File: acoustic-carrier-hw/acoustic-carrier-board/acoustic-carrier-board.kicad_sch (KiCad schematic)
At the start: 0 parts

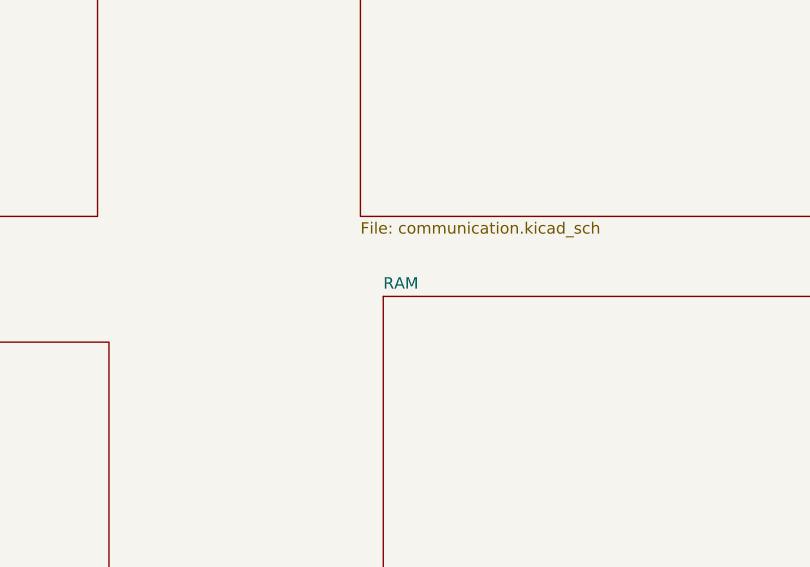
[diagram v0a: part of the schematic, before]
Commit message: [carrier] Finished ethernet
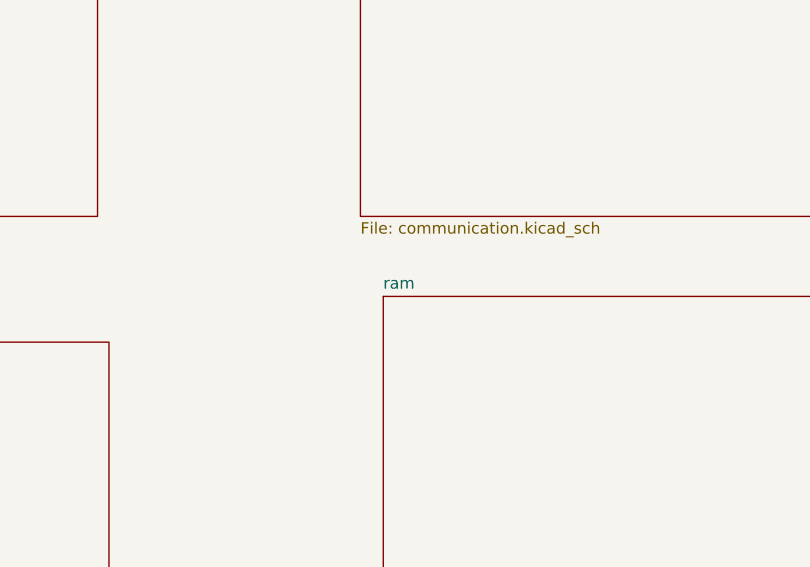
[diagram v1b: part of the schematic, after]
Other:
- sheet RAM renamed ram
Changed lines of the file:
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@@
 			(color 0 0 0 0.0000)
 		)
-		(property "Sheetname" "RAM"
+		(property "Sheetname" "ram"
 			(at 177.8 122.4784 0)
 			(effects

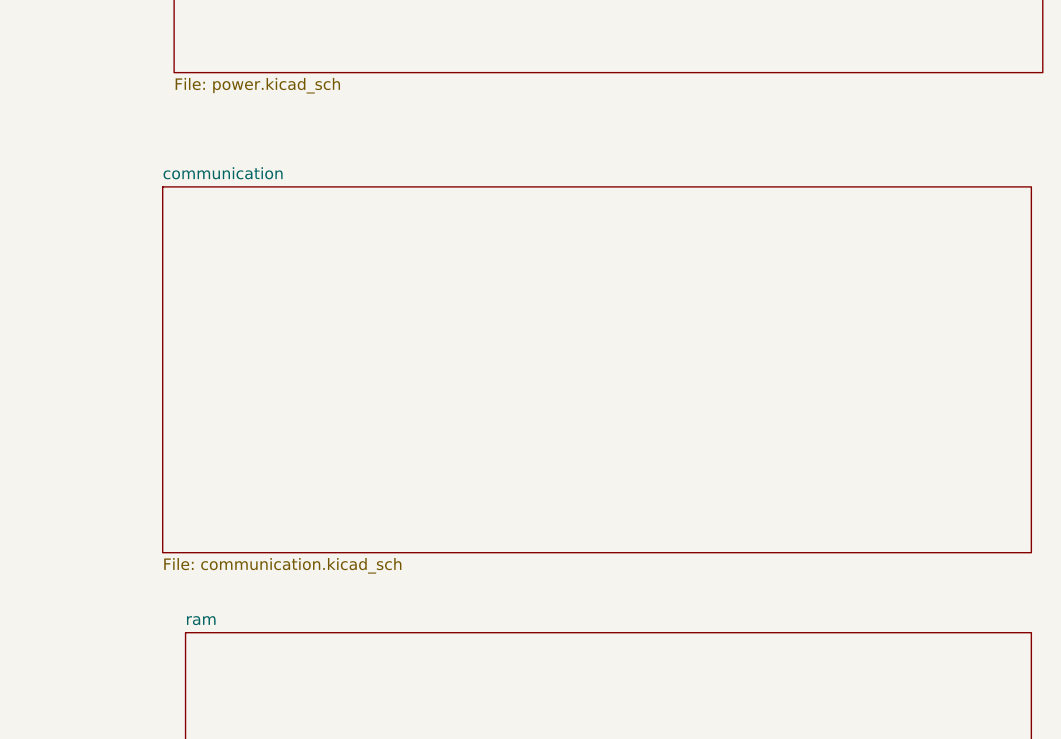
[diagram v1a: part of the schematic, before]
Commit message: [carrier] Fixed most of the carrier board ERC issues (next) fix BGA ERC issue
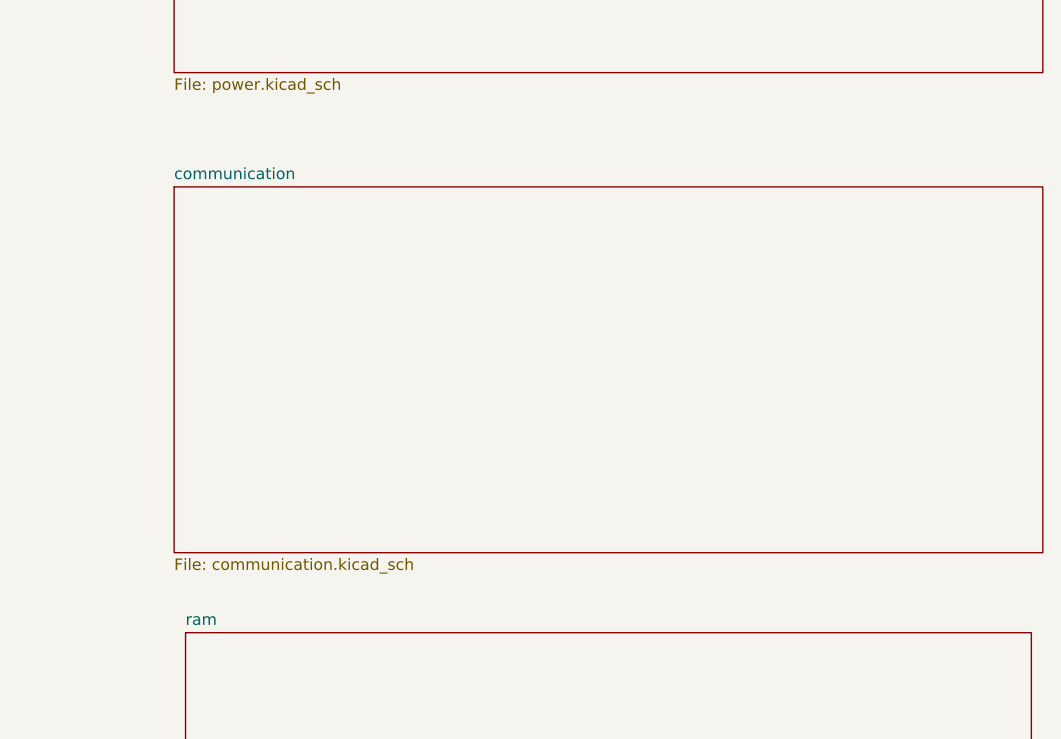
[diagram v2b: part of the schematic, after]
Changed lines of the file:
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@@
 	)
 	(sheet
-		(at 175.26 73.66)
+		(at 176.53 73.66)
 		(size 96.52 40.64)
 		(exclude_from_sim no)
@@
 		)
 		(property "Sheetname" "communication"
-			(at 175.26 72.9484 0)
+			(at 176.53 72.9484 0)
 			(effects
 				(font
@@
 		)
 		(property "Sheetfile" "communication.kicad_sch"
-			(at 175.26 114.8846 0)
+			(at 176.53 114.8846 0)
 			(effects
 				(font
@@
 		)
 		(property "Field2" ""
-			(at 175.26 73.66 0)
+			(at 176.53 73.66 0)
 			(effects
 				(font

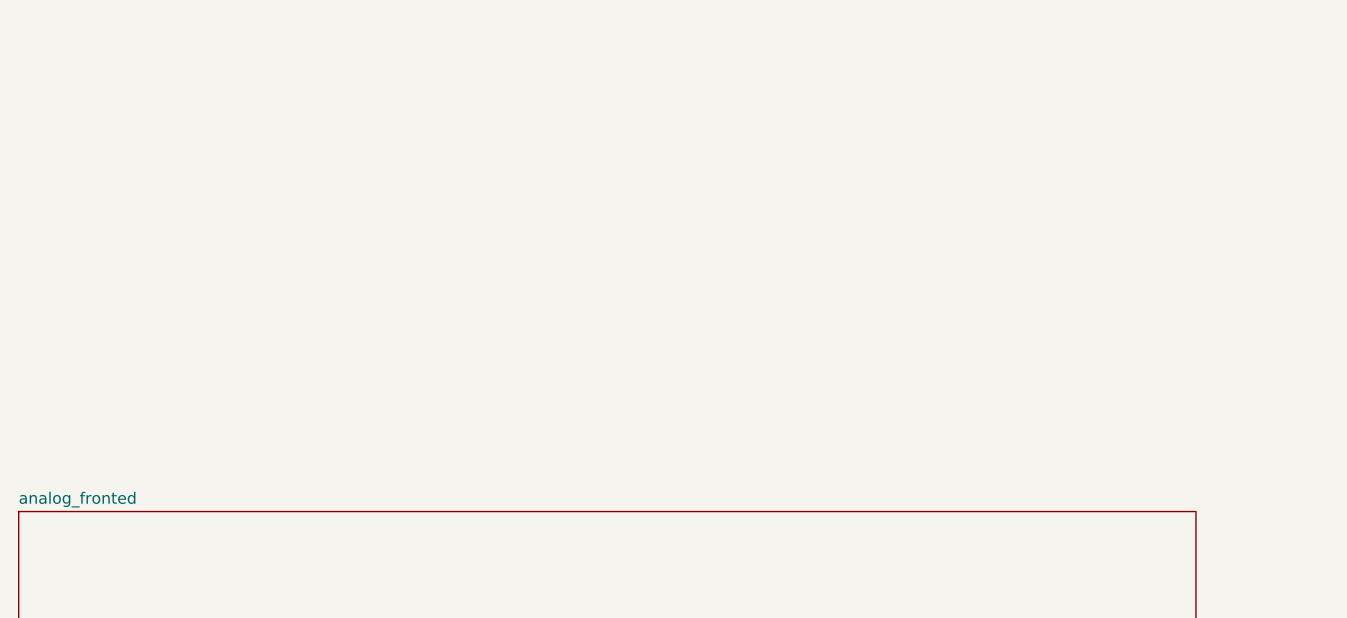
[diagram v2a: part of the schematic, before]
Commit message: [carrier] Fixed ERC errors and fpga-footprints (next) ) add extra pin functionality to 2 remaining banks, perform schematic checks
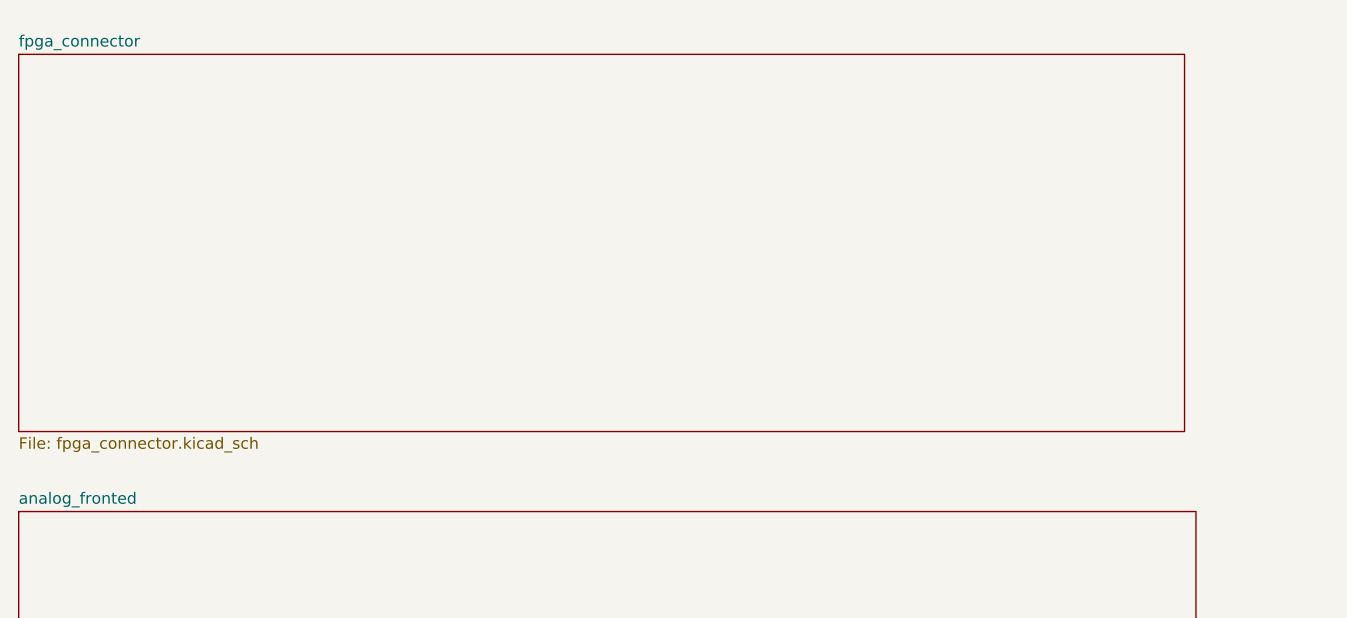
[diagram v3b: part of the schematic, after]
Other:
- added sheet fpga_connector (fpga_connector.kicad_sch)
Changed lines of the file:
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@@
+	)
+	(sheet
+		(at 15.24 24.13)
+		(size 129.54 41.91)
+		(exclude_from_sim no)
+		(in_bom yes)
+		(on_board yes)
+		(dnp no)
+		(fields_autoplaced yes)
+		(stroke
+			(width 0.1524)
+			(type solid)
+		)
+		(fill
+			(color 0 0 0 0.0000)
+		)
+		(property "Sheetname" "fpga_connector"
+			(at 15.24 23.4184 0)
+			(effects
+				(font
+					(size 1.27 1.27)
+				)
+				(justify left bottom)
+			)
+		)
+		(property "Sheetfile" "fpga_connector.kicad_sch"
+			(at 15.24 66.6246 0)
+			(effects
+				(font
+					(size 1.27 1.27)
+				)
+				(justify left top)
+			)
+		)
+		(instances
+			(project "acoustic-carrier-board"
+				(path "/25b015c9-ab13-4427-b72c-b6f348597100"
+					(page "8")
+				)
+			)
+		)
 	)
 	(sheet

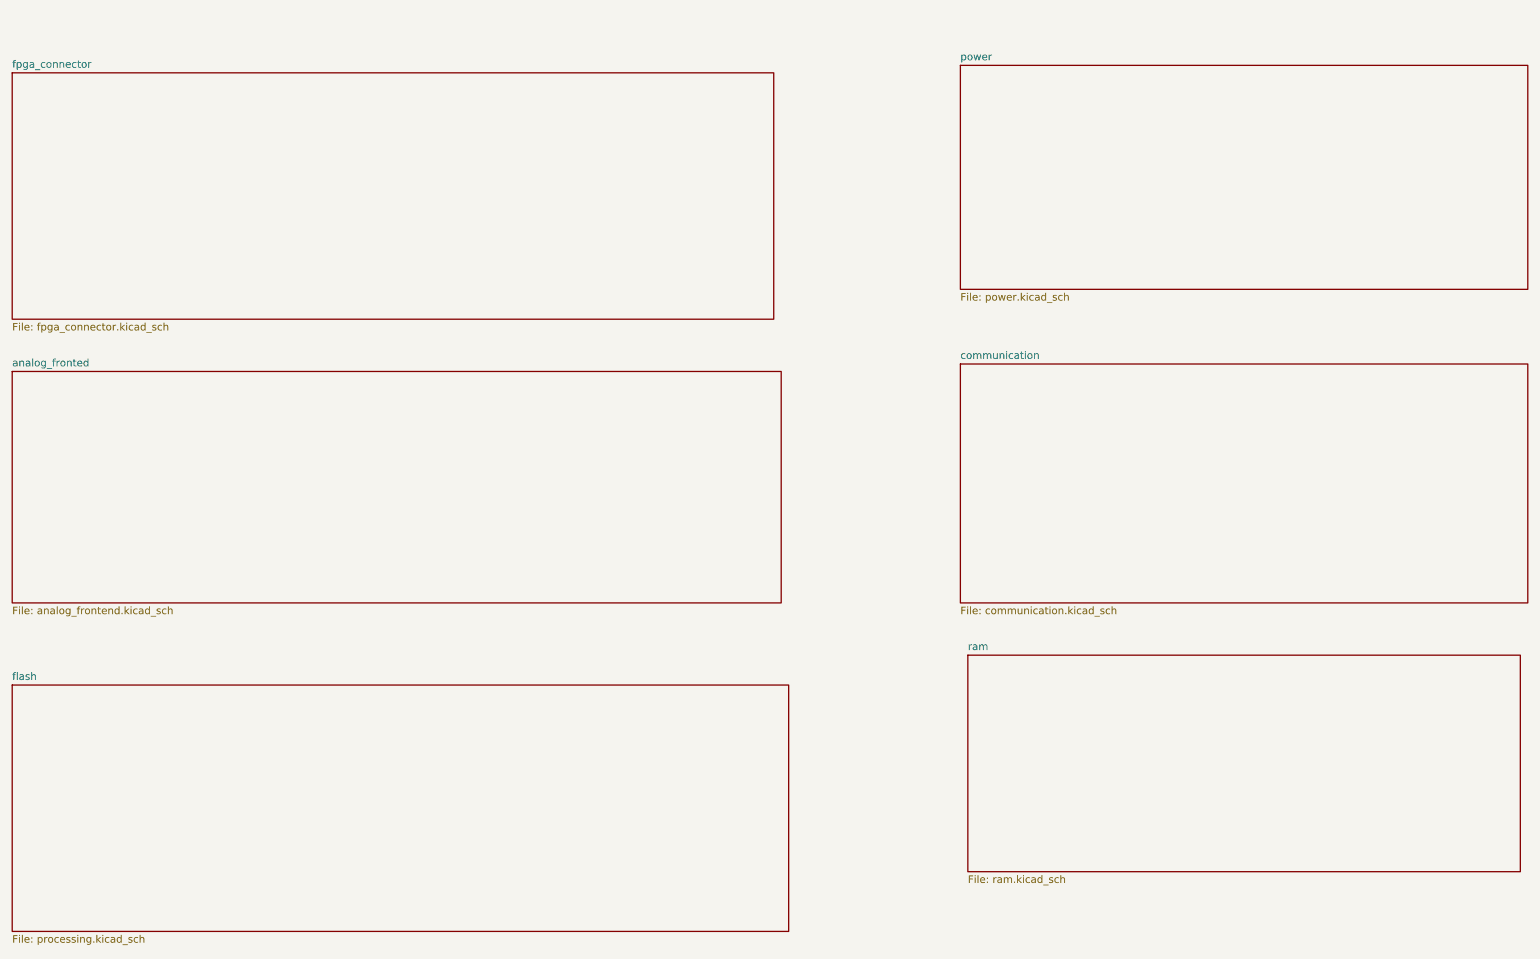
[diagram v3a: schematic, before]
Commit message: [carrier] Started tina simulations with th4521
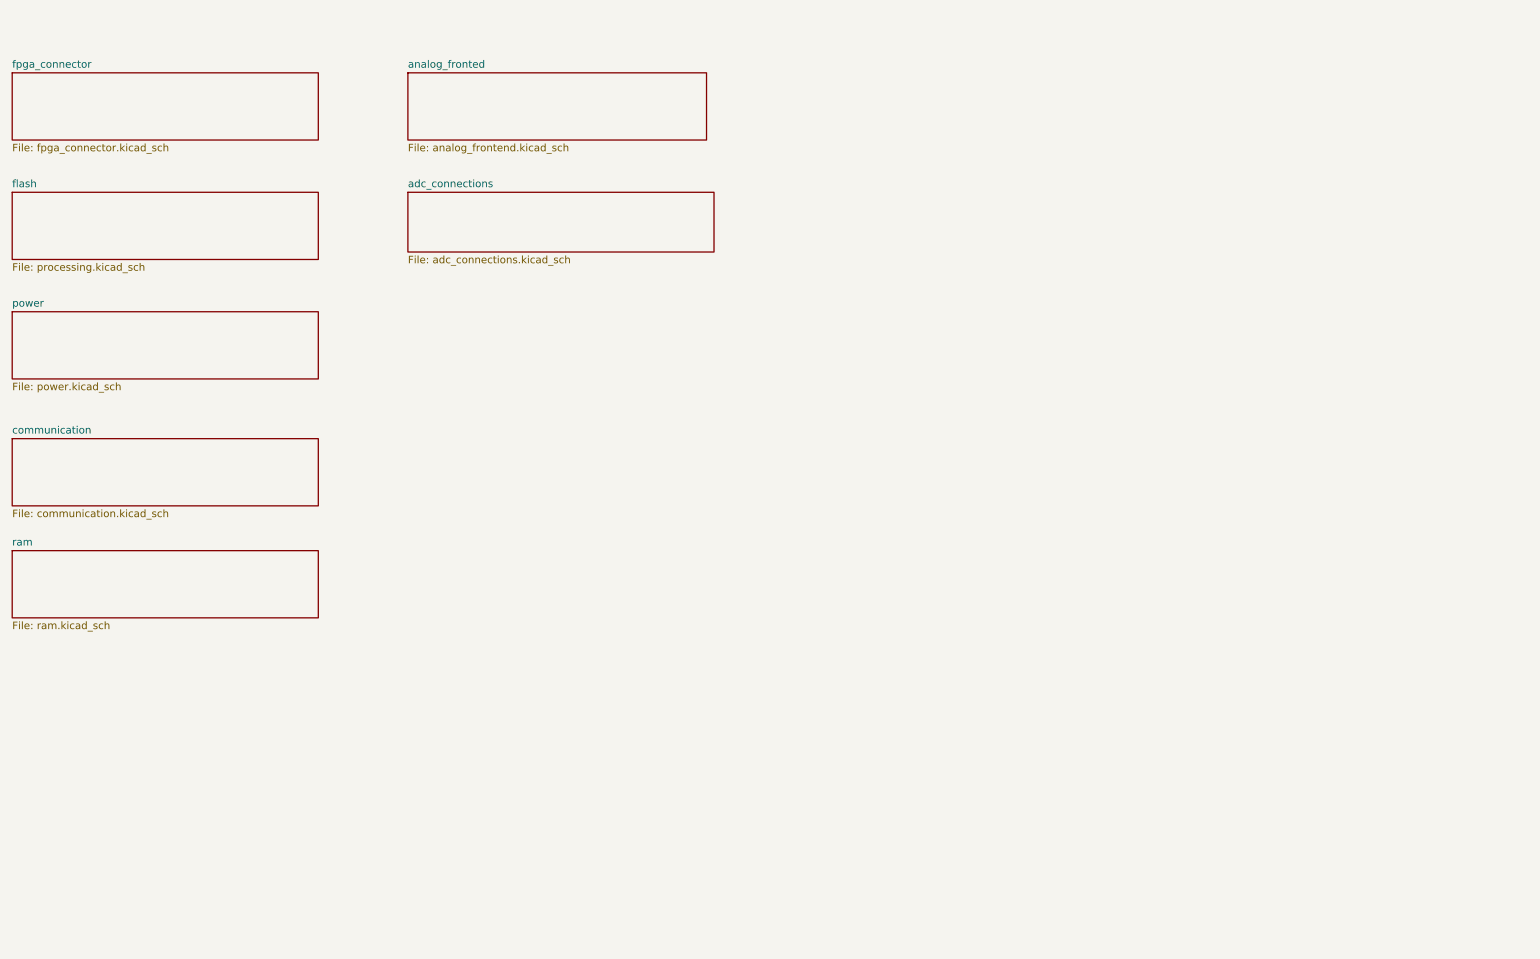
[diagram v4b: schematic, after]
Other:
- added sheet adc_connections (adc_connections.kicad_sch)
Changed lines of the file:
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@@
 	(paper "A4")
 	(sheet
-		(at 15.24 74.93)
-		(size 130.81 39.37)
+		(at 82.55 24.13)
+		(size 50.8 11.43)
 		(exclude_from_sim no)
 		(in_bom yes)
@@
 		)
 		(property "Sheetname" "analog_fronted"
-			(at 15.24 74.2184 0)
+			(at 82.55 23.4184 0)
 			(effects
 				(font
@@
 		)
 		(property "Sheetfile" "analog_frontend.kicad_sch"
-			(at 15.24 114.8846 0)
+			(at 82.55 36.1446 0)
 			(effects
 				(font
@@
 	)
 	(sheet
-		(at 15.24 128.27)
-		(size 132.08 41.91)
+		(at 15.24 44.45)
+		(size 52.07 11.43)
 		(exclude_from_sim no)
 		(in_bom yes)
@@
 		)
 		(property "Sheetname" "flash"
-			(at 15.24 127.5584 0)
+			(at 15.24 43.7384 0)
 			(effects
 				(font
@@
 		)
 		(property "Sheetfile" "processing.kicad_sch"
-			(at 15.24 170.7646 0)
+			(at 15.24 56.4646 0)
 			(effects
 				(font
@@
 	)
 	(sheet
-		(at 176.53 22.86)
-		(size 96.52 38.1)
+		(at 82.55 44.45)
+		(size 52.07 10.16)
+		(exclude_from_sim no)
+		(in_bom yes)
+		(on_board yes)
+		(dnp no)
+		(fields_autoplaced yes)
+		(stroke
+			(width 0.1524)
+			(type solid)
+		)
+		(fill
+			(color 0 0 0 0.0000)
+		)
+		(property "Sheetname" "adc_connections"
+			(at 82.55 43.7384 0)
+			(effects
+				(font
+					(size 1.27 1.27)
+				)
+				(justify left bottom)
+			)
+		)
+		(property "Sheetfile" "adc_connections.kicad_sch"
+			(at 82.55 55.1946 0)
+			(effects
+				(font
+					(size 1.27 1.27)
+				)
+				(justify left top)
+			)
+		)
+		(instances
+			(project "acoustic-carrier-board"
+				(path "/25b015c9-ab13-4427-b72c-b6f348597100"
+					(page "2")
+				)
+			)
+		)
+	)
+	(sheet
+		(at 15.24 64.77)
+		(size 52.07 11.43)
 		(exclude_from_sim no)
 		(in_bom yes)
@@
 		)
 		(property "Sheetname" "power"
-			(at 176.53 22.1484 0)
+			(at 15.24 64.0584 0)
 			(effects
 				(font
@@
 		)
 		(property "Sheetfile" "power.kicad_sch"
-			(at 176.53 61.5446 0)
+			(at 15.24 76.7846 0)
 			(effects
 				(font
@@
 		)
 		(property "Field2" ""
-			(at 176.53 22.86 0)
+			(at 15.24 64.77 0)
 			(effects
 				(font
@@
 	(sheet
 		(at 15.24 24.13)
-		(size 129.54 41.91)
+		(size 52.07 11.43)
 		(exclude_from_sim no)
 		(in_bom yes)
@@
 		)
 		(property "Sheetfile" "fpga_connector.kicad_sch"
-			(at 15.24 66.6246 0)
+			(at 15.24 36.1446 0)
 			(effects
 				(font
@@
 	)
 	(sheet
-		(at 176.53 73.66)
-		(size 96.52 40.64)
+		(at 15.24 86.36)
+		(size 52.07 11.43)
 		(exclude_from_sim no)
 		(in_bom yes)
@@
 		)
 		(property "Sheetname" "communication"
-			(at 176.53 72.9484 0)
+			(at 15.24 85.6484 0)
 			(effects
 				(font
@@
 		)
 		(property "Sheetfile" "communication.kicad_sch"
-			(at 176.53 114.8846 0)
+			(at 15.24 98.3746 0)
 			(effects
 				(font
@@
 		)
 		(property "Field2" ""
-			(at 176.53 73.66 0)
+			(at 15.24 86.36 0)
 			(effects
 				(font
@@
 	)
 	(sheet
-		(at 177.8 123.19)
-		(size 93.98 36.83)
+		(at 15.24 105.41)
+		(size 52.07 11.43)
 		(exclude_from_sim no)
 		(in_bom yes)
@@
 		)
 		(property "Sheetname" "ram"
-			(at 177.8 122.4784 0)
+			(at 15.24 104.6984 0)
 			(effects
 				(font
@@
 		)
 		(property "Sheetfile" "ram.kicad_sch"
-			(at 177.8 160.6046 0)
+			(at 15.24 117.4246 0)
 			(effects
 				(font
@@
 		)
 		(property "Field2" ""
-			(at 177.8 123.19 0)
-			(effects
-				(font
+			(at 15.24 105.41 0)
+			(effects
+				(font

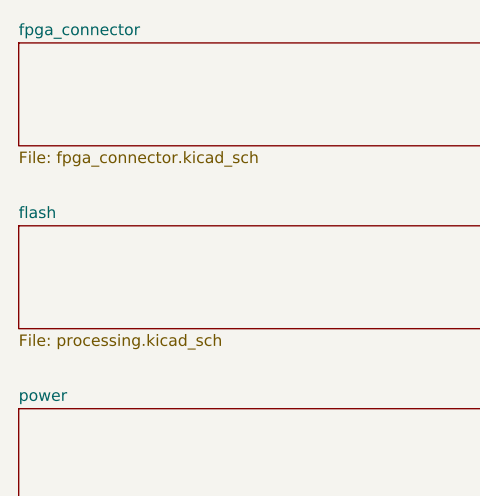
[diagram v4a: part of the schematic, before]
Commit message: [carrier] Finished flash and config check
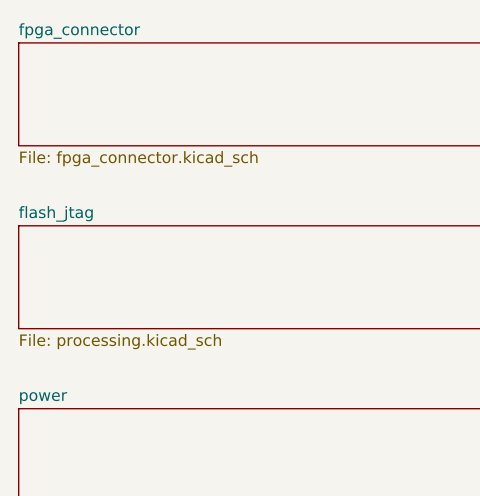
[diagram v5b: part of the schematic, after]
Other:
- sheet flash renamed flash_jtag
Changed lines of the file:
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@@
 			(color 0 0 0 0.0000)
 		)
-		(property "Sheetname" "flash"
+		(property "Sheetname" "flash_jtag"
 			(at 15.24 43.7384 0)
 			(effects
